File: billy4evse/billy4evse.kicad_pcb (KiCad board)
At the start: 2 copper layers, 49.7 x 86.4 mm, 31 parts, among them J1 Conn_01x02, J2 Screw_Terminal_01x02, J3 Conn_01x12, J4 Conn_01x12, J5 AudioJack3, J6 AudioJack3, J7 USB_B_Micro, J8 AudioJack3, U1 LoPy, U2 CH340C

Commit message: billy{sch, pcb}: Add GPIO headers
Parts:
- removed J4: Conn_01x12, Connector_PinHeader_2.54mm:PinHeader_1x12_P2.54mm_Vertical
- J3: value Conn_01x12 -> Conn_02x06_Odd_Even; footprint Connector_PinHeader_2.54mm:PinHeader_1x12_P2.54mm_Vertical -> Connector_PinHeader_2.54mm:PinHeader_2x06_P2.54mm_Vertical
- moved J3 85.4 mm to (128.9, 103.7), turned to 90 degrees
- moved D2 1.80 mm to (137.0, 114.3)
- moved R8 1.80 mm to (137.0, 117.8)
- moved D1 1.20 mm to (135.5, 114.3)
- moved R7 1.20 mm to (135.5, 117.8)
- moved J7 0.10 mm to (127.0, 131.3)
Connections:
- J3 pad 10: /P12 -> /P14
- J3 pad 3: /P2 -> /P8
- J3 pad 4: /P3 -> /P21
- J3 pad 5: /P4 -> /P9
- J3 pad 6: /P8 -> /P20
- J3 pad 7: /P9 -> /P10
- J3 pad 8: /P10 -> /P19
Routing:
- net /P21: track 0.00 -> 42.2 mm
- net /P20: track 0.00 -> 38.6 mm
- net /P19: track 0.00 -> 35.0 mm
- net /P14: track 0.00 -> 29.2 mm
- net /P8: track 0.00 -> 22.2 mm
- net /P9: track 0.00 -> 18.6 mm
- net /P10: track 0.00 -> 15.4 mm
- net /P11: track 0.00 -> 10.5 mm
- net +3V3: track 87.7 -> 97.0 mm
- net /LOPY2USB: track 49.6 -> 55.5 mm
- net /USB2LOPY: track 51.4 -> 55.9 mm
- net +5V: track 108.7 -> 105.4 mm
- net GND: vias 73 -> 78
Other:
- outline, holes or cut-outs redrawn
- board text added: "100-240 VAC"
- board text added: "P19"
- board text removed: "P12"
- board text removed: "P13"
- board text removed: "P16"
- board text removed: "P18"
- board text removed: "P2"
- board text removed: "P22"
- board text removed: "P23"
- board text removed: "P3"
- board text removed: "P4"

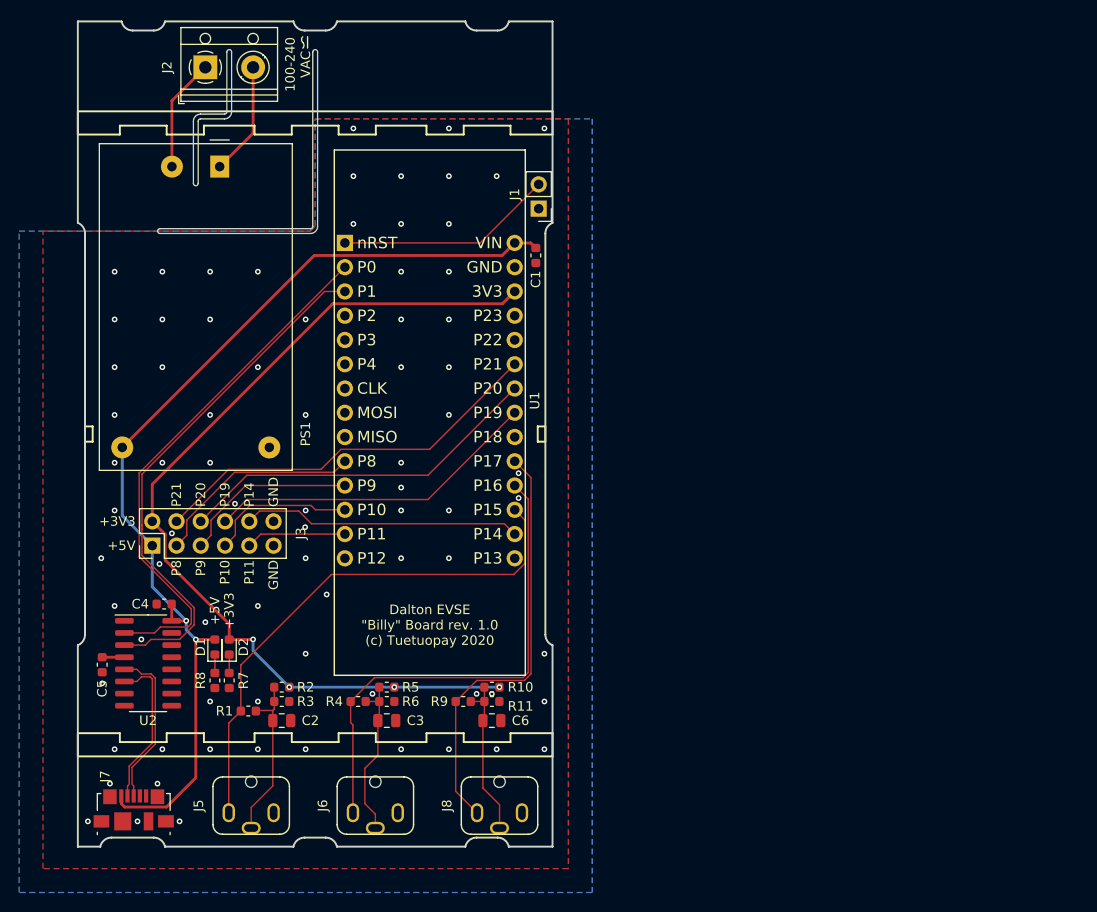
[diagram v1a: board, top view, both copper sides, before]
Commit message: billy{sch, pcb}: Add screw terminals on top for current sensors
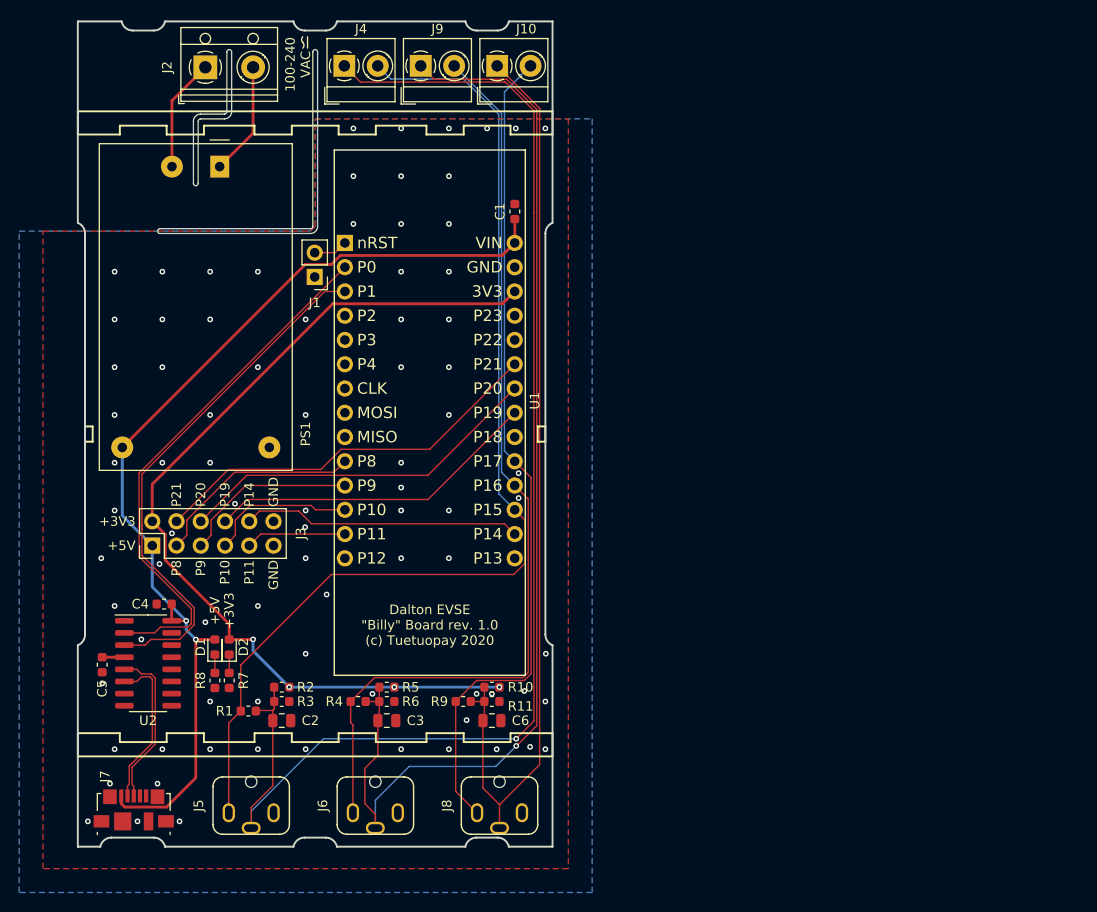
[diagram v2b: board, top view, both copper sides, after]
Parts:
- added J10: Screw_Terminal_01x02, TerminalBlock_MetzConnect:TerminalBlock_MetzConnect_Type059_RT06302HBWC_1x02_P3.50mm_Horizontal, F.Cu at (165.1, 53.5)
- added J4: Screw_Terminal_01x02, TerminalBlock_MetzConnect:TerminalBlock_MetzConnect_Type059_RT06302HBWC_1x02_P3.50mm_Horizontal, F.Cu at (149.1, 53.5)
- added J9: Screw_Terminal_01x02, TerminalBlock_MetzConnect:TerminalBlock_MetzConnect_Type059_RT06302HBWC_1x02_P3.50mm_Horizontal, F.Cu at (157.1, 53.5)
- moved J1 24.5 mm to (145.9, 75.5)
- moved C1 5.10 mm to (166.9, 68.7), turned to 270 degrees
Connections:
- U1 pad 14: /P12 -> (no net)
- U1 pad 15: /P13 -> (no net)
- U1 pad 20: /P18 -> (no net)
- U1 pad 24: /P22 -> (no net)
- U1 pad 25: /P23 -> (no net)
- U1 pad 4: /P2 -> (no net)
- U1 pad 5: /P3 -> (no net)
- U1 pad 6: /P4 -> (no net)
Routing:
- net Net-(C2-Pad2): track 17.6 -> 138.5 mm, vias 0 -> 1
- net Net-(C3-Pad2): track 17.3 -> 118.8 mm, vias 0 -> 1
- net Net-(C6-Pad2): track 17.0 -> 97.9 mm
- net /CT0: track 56.2 -> 113.1 mm
- net /CT1: track 51.8 -> 98.3 mm
- net /CT2: track 44.6 -> 87.6 mm
- net Net-(J1-Pad2): track 22.8 -> 3.58 mm
- net GND: vias 78 -> 83

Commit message: billy: Add clamping diodes to sensor inputs
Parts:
- added D3: BAT54S, Package_TO_SOT_SMD:SOT-23, F.Cu at (142.5, 116.0)
- added D4: BAT54S, Package_TO_SOT_SMD:SOT-23, F.Cu at (146.0, 116.0)
- added D5: BAT54S, Package_TO_SOT_SMD:SOT-23, F.Cu at (158.8, 121.4)
- moved J2 3.54 mm to (131.0, 54.1)
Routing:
- net +3V3: track 97.0 -> 105.4 mm
- net /CT1: track 98.3 -> 103.4 mm
- net /AC_N: track 11.8 -> 9.90 mm
- net /AC_L: track 11.8 -> 9.90 mm
- net /CT2: track 87.6 -> 88.4 mm
- net /CT0: track 113.1 -> 113.6 mm
- net GND: vias 83 -> 82
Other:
- outline, holes or cut-outs redrawn

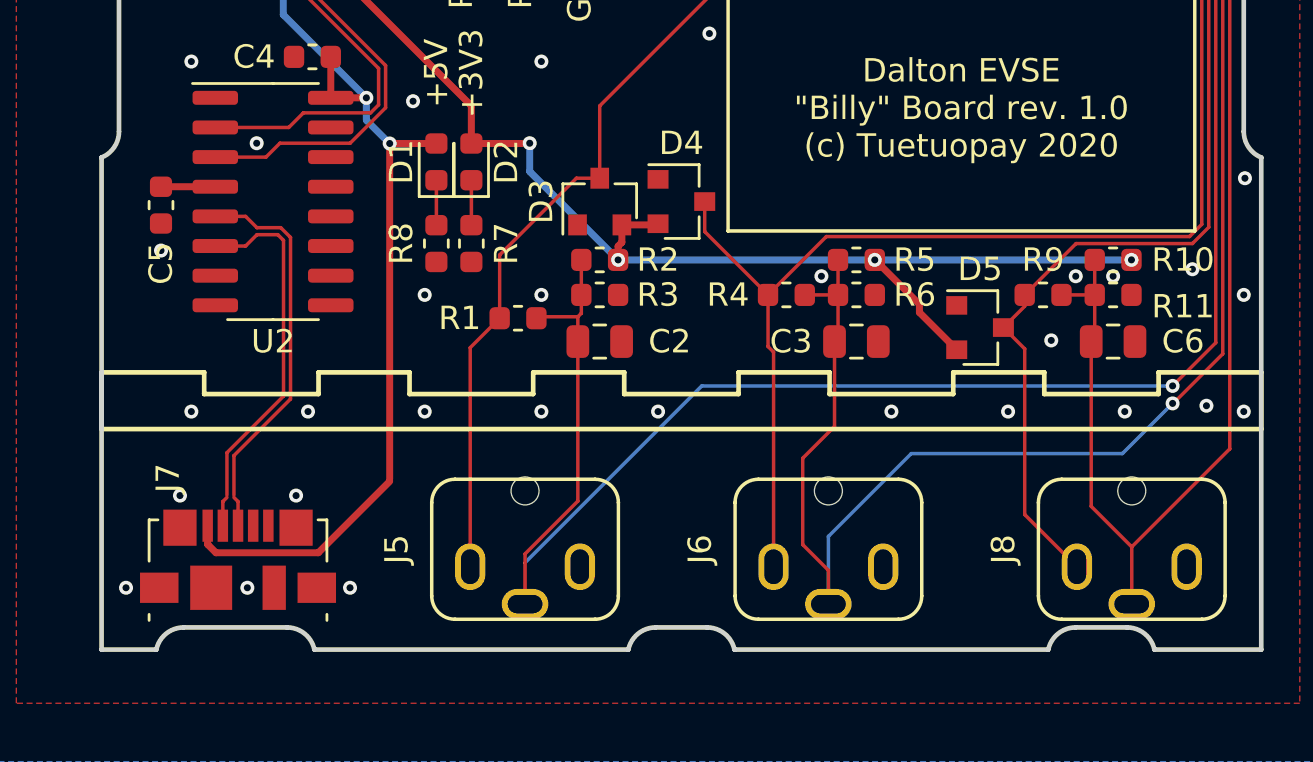
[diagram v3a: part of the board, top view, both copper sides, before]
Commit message: billy: Switch USB connector for vertical connector
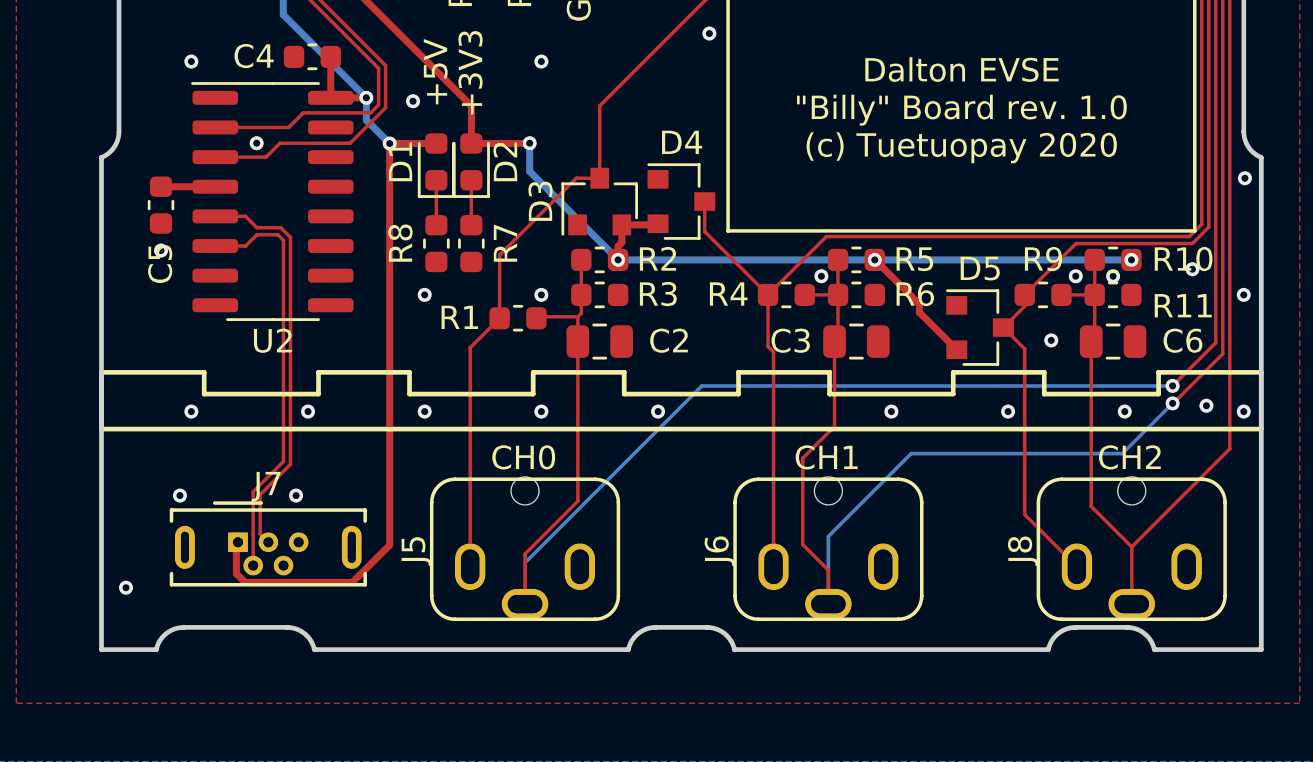
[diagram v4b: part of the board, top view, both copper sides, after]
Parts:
- J7: footprint Connector_USB:USB_Micro-B_Molex_47346-0001 -> Connector_USB:USB_Micro-B_Wuerth_614105150721_Vertical
- moved J7 0.75 mm to (127.0, 130.6)
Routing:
- net +5V: track 105.4 -> 107.0 mm
- net /USB_N: track 16.4 -> 17.7 mm
- net GND: vias 82 -> 80
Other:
- board text added: "CH0"
- board text added: "CH1"
- board text added: "CH2"
- board text added: "J7 - Würth 614105150721 - Korean Hroparts Elec U-D-M5DD-W-1"
